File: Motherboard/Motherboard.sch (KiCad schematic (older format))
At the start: 0 parts

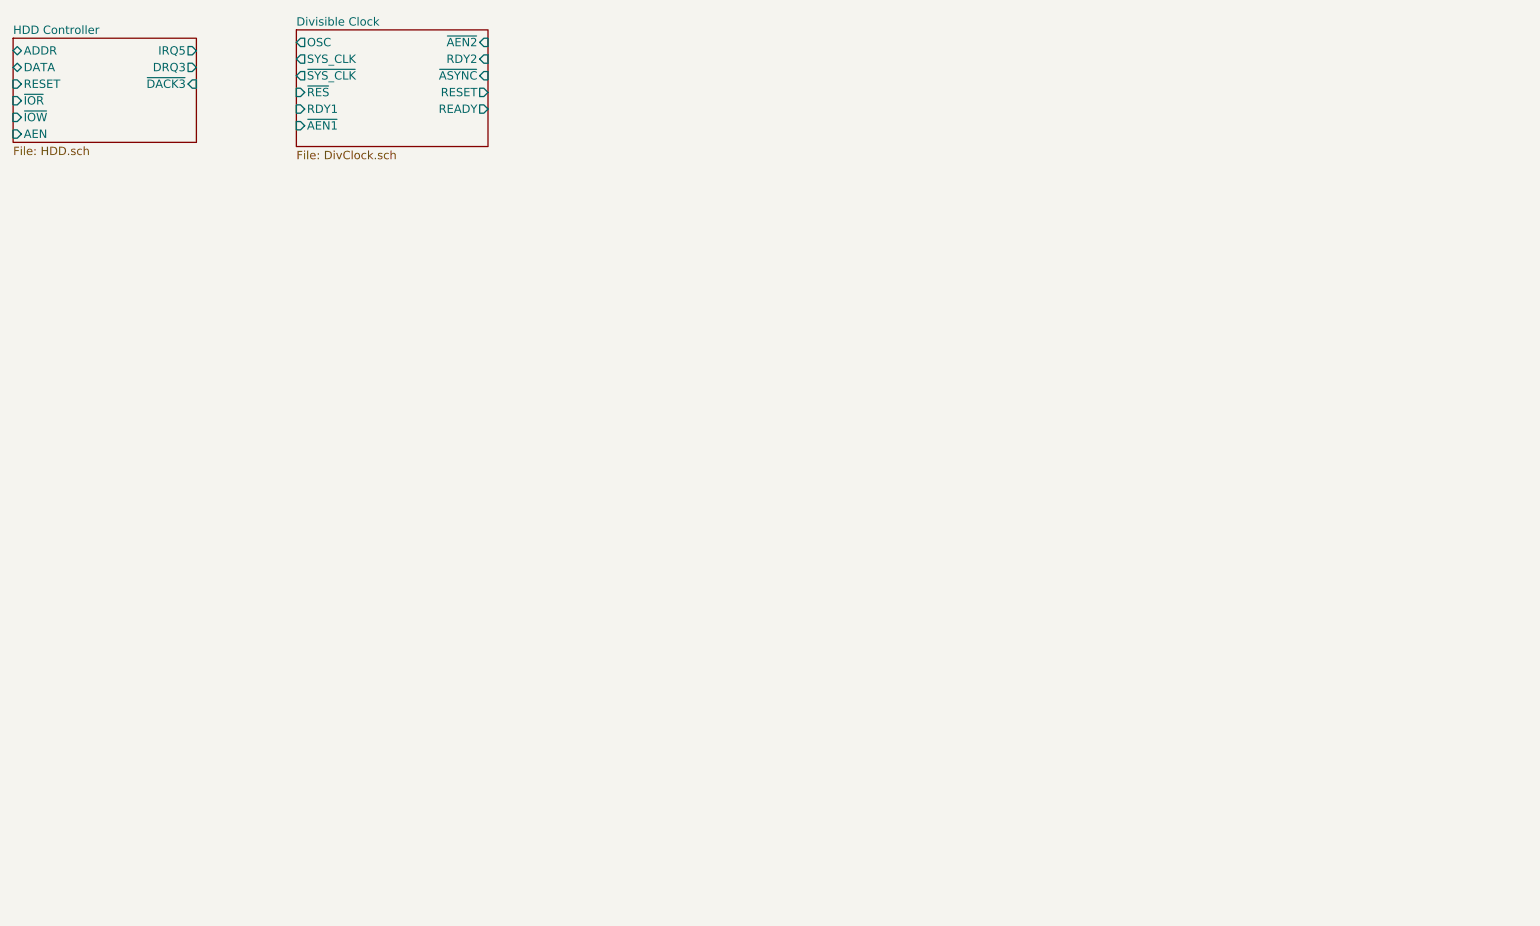
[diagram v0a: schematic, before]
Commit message: More work on Motherboard
Began work on PCB Routing
Began work on DMA
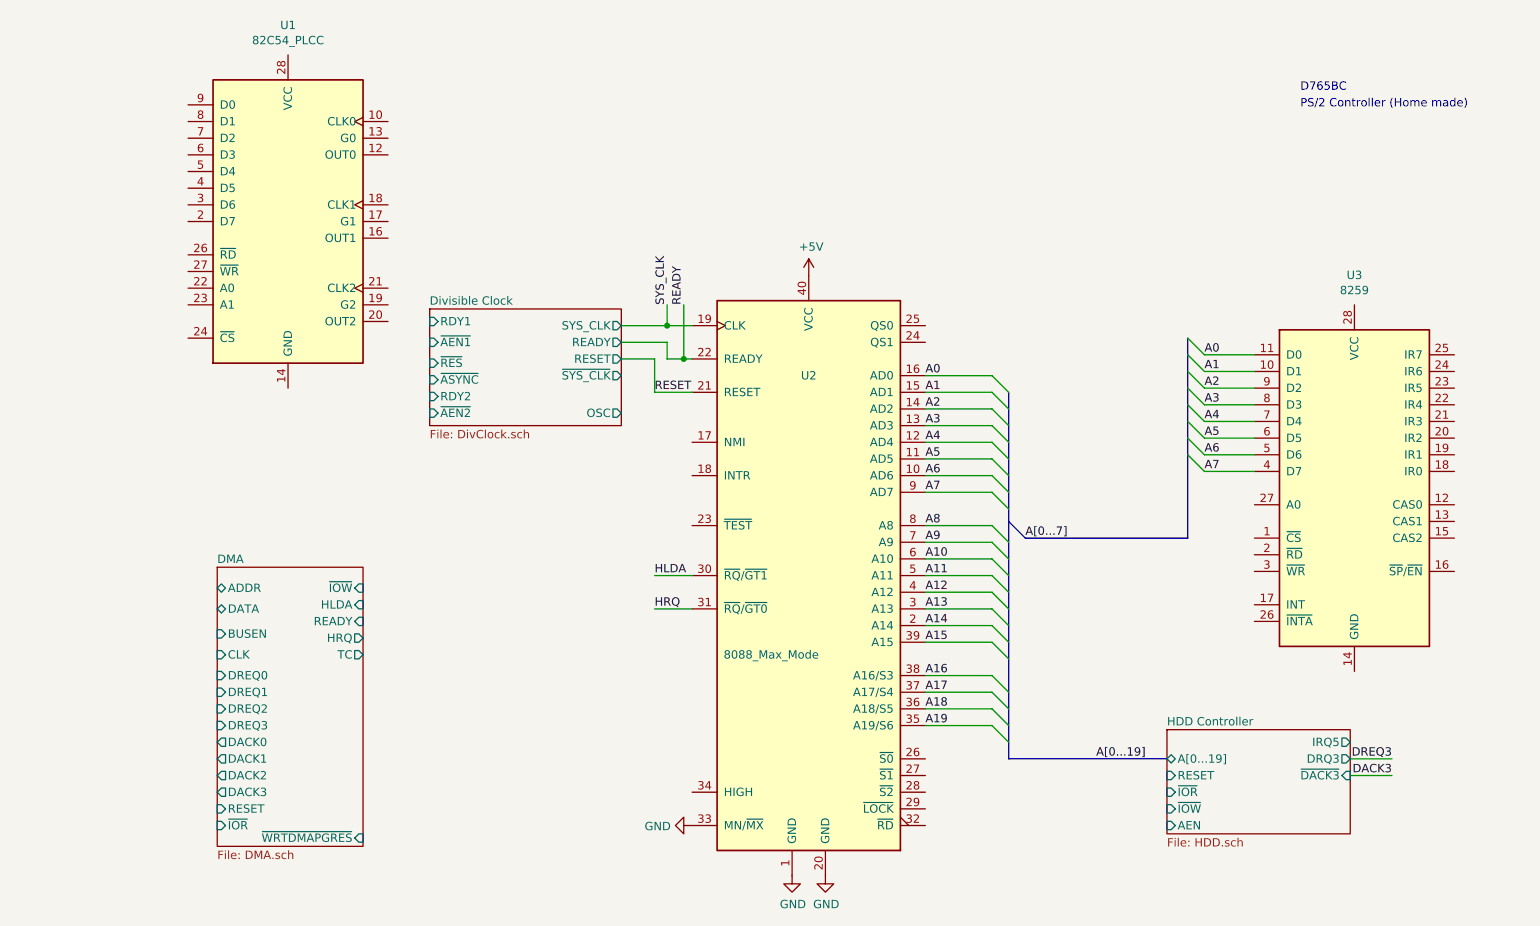
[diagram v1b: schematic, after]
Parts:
- added U1: 82C54_PLCC, Housings_DIP:DIP-28_W15.24mm_Socket, symbol Timer:82C54_PLCC
- added U2: 8088_Max_Mode, Housings_DIP:DIP-40_W15.24mm_Socket, symbol MCU_Intel:8088_Max_Mode
- added U3: 8259, Housings_DIP:DIP-28_W7.62mm_Socket, symbol Interface:8259
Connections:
- new net +5V: U2.40 (VCC)
- new net A0: U2.16 (AD0), U3.11 (D0)
- new net A1: U2.15 (AD1), U3.10 (D1)
- new net A10: U2.6 (A10)
- new net A11: U2.5 (A11)
- new net A12: U2.4 (A12)
- new net A13: U2.3 (A13)
- new net A14: U2.2 (A14)
- new net A15: U2.39 (A15)
- new net A16: U2.38 (A16/S3)
- new net A17: U2.37 (A17/S4)
- new net A18: U2.36 (A18/S5)
- new net A19: U2.35 (A19/S6)
- new net A2: U2.14 (AD2), U3.9 (D2)
- new net A3: U2.13 (AD3), U3.8 (D3)
- new net A4: U2.12 (AD4), U3.7 (D4)
- new net A5: U2.11 (AD5), U3.6 (D5)
- new net A6: U2.10 (AD6), U3.5 (D6)
- new net A7: U2.9 (AD7), U3.4 (D7)
- new net A8: U2.8 (A8)
- new net A9: U2.7 (A9)
- new net GND: U2.1 (GND), U2.20 (GND), U2.33 (MN/~MX~)
- new net HLDA: U2.30 (~RQ~/~GT1~)
- new net HRQ: U2.31 (~RQ~/~GT0~)
- new net READY: U2.22 (READY)
- new net RESET: U2.21 (RESET)
- new net SYS_CLK: U2.19 (CLK)
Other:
- note added: "D765BC"
- note added: "PS/2 Controller (Home made)"

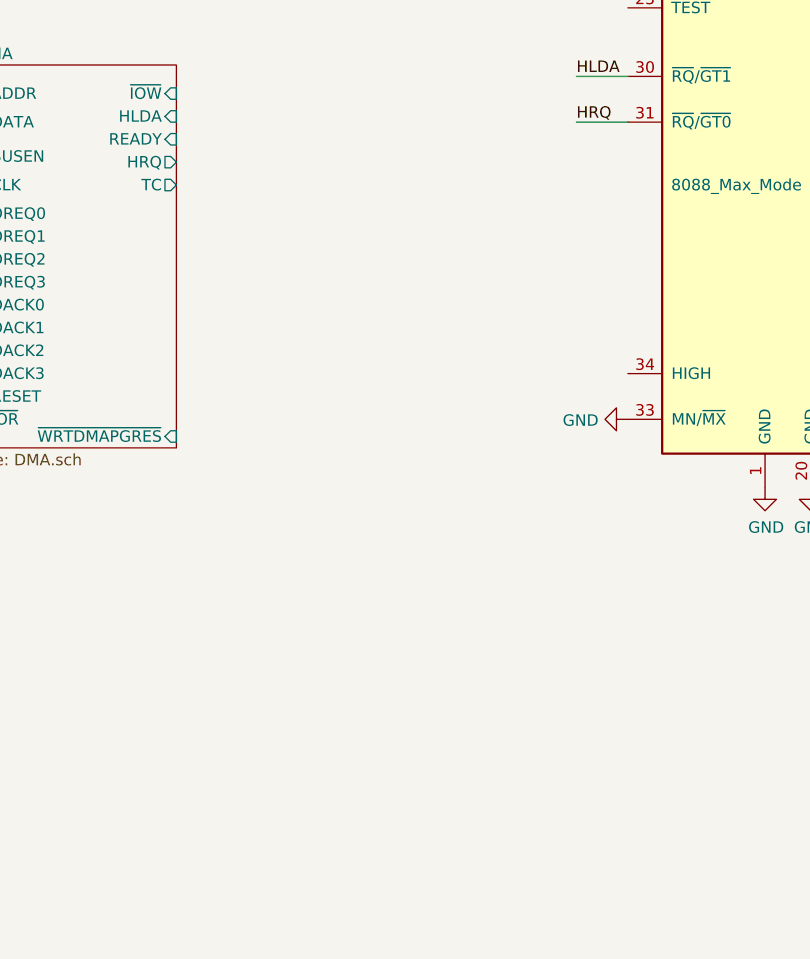
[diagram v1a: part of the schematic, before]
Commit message: Added ISA Footprint
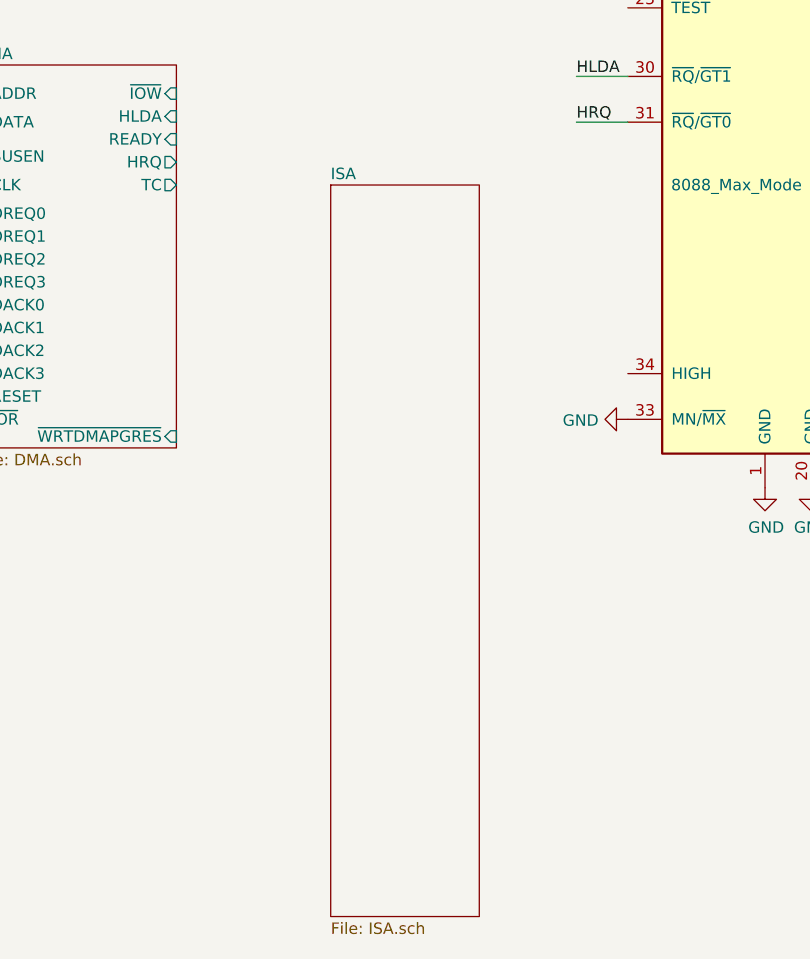
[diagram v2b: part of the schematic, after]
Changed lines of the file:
@@
 $Descr A4 11693 8268
 encoding utf-8
-Sheet 1 4
+Sheet 1 5
 Title "XT Clone Motherboard"
 Date ""
@@
 Wire Bus Line
 	6950 5100 7900 5100
+Text Label 7475 5100 0    50   ~ 0
+A[0...19]
+$Sheet
+S 3750 4475 650  3200
+U 5C18FA46
+F0 "ISA" 50
+F1 "ISA.sch" 50
+$EndSheet
 Wire Bus Line
 	8025 2575 8025 3775
 Wire Bus Line
 	6950 2900 6950 5100
-Text Label 7475 5100 0    50   ~ 0
-A[0...19]
 $EndSCHEMATC

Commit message: A VERY large sync...
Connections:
- net IO-Decoder/~S0: now reaches U2.26 (~S0~)
- net IO-Decoder/~S1: now reaches U2.27 (~S1~)
- net IO-Decoder/~S2: now reaches U2.28 (~S2~)
- net ~INTA: now reaches U3.26 (~INTA~)
- net A0 renamed AD0
- net AD0: no longer U3.11 (D0)
- net A1 renamed AD1
- net AD1: no longer U3.10 (D1)
- net A10 renamed AD10
- net A11 renamed AD11
- net A12 renamed AD12
- net A13 renamed AD13
- net A14 renamed AD14
- net A15 renamed AD15
- net A16 renamed AD16
- net A17 renamed AD17
- net A18 renamed AD18
- net A19 renamed AD19
- net A2 renamed AD2
- net AD2: no longer U3.9 (D2)
- net A3 renamed AD3
- net AD3: no longer U3.8 (D3)
- net A4 renamed AD4
- net AD4: no longer U3.7 (D4)
- net A5 renamed AD5
- net AD5: no longer U3.6 (D5)
- net A6 renamed AD6
- net AD6: no longer U3.5 (D6)
- net A7 renamed AD7
- net AD7: no longer U3.4 (D7)
- net A8 renamed AD8
- net A9 renamed AD9
- new net D0: U3.11 (D0)
- new net D1: U3.10 (D1)
- new net D2: U3.9 (D2)
- new net D3: U3.8 (D3)
- new net D4: U3.7 (D4)
- new net D5: U3.6 (D5)
- new net D6: U3.5 (D6)
- new net D7: U3.4 (D7)
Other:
- note added: "DCLK From IO Decode"
- moved on the sheet: U1, U3

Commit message: Large sync
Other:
- note removed: "D765BC"
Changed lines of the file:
@@
 EELAYER 26 0
 EELAYER END
-$Descr A4 11693 8268
+$Descr A3 16535 11693
 encoding utf-8
 Sheet 1 8
@@
 $EndDescr
 $Sheet
-S 9325 4200 1100 625
+S 8400 4650 1100 625
 U 5C0ABBCC
 F0 "HDD Controller" 50
 F1 "HDD.sch" 50
-F2 "RESET" I L 9325 4475 50
-F3 "~IOR" I L 9325 4575 50
-F4 "~IOW" I L 9325 4675 50
-F5 "AEN" I L 9325 4775 50
-F6 "IRQ5" O R 10425 4275 50
-F7 "DRQ3" O R 10425 4375 50
-F8 "~DACK3" I R 10425 4475 50
-F9 "A[0...19]" B L 9325 4375 50
+F2 "RESET" I L 8400 4925 50
+F3 "~IOR" I L 8400 5025 50
+F4 "~IOW" I L 8400 5125 50
+F5 "AEN" I L 8400 5225 50
+F6 "IRQ5" O R 9500 4725 50
+F7 "DRQ3" O R 9500 4825 50
+F8 "~DACK3" I R 9500 4925 50
+F9 "A[0...19]" B L 8400 4825 50
 $EndSheet
 $Sheet
@@
 	1    0    0    -1
 $EndComp
-Text Notes 8700 1100 0    50   ~ 0
-D765BC
 Text Notes 8700 1200 0    50   ~ 0
 PS/2 Controller (Home made)
-Text Label 10675 4375 2    50   ~ 0
+Text Label 9750 4825 2    50   ~ 0
 DREQ3
 Wire Wire Line
-	10425 4375 10675 4375
+	9500 4825 9750 4825
 Wire Wire Line
 	4900 2500 4900 2375
@@
 SYS_CLK
 Wire Wire Line
-	10425 4475 10675 4475
-Text Label 10675 4475 2    50   ~ 0
+	9500 4925 9750 4925
+Text Label 9750 4925 2    50   ~ 0
 DACK3
 Text Label 4825 2900 0    50   ~ 0
@@
 F16 "D[0...7]" O R 7875 5800 50
 F17 "A[0...19]" O R 7875 5700 50
+F18 "DCLK" O R 7875 5900 50
 $EndSheet
 Wire Bus Line
@@
 A[0...19]
 Text Label 9450 3050 1    50   ~ 0
-D[0...7]
+XD[0...7]
+Text Notes 975  4450 0    50   ~ 0
+DCLK From IO Decode
+Wire Wire Line
+	7875 5900 8275 5900
 Wire Bus Line
 	1050 4075 2200 4075
@@
 Wire Bus Line
 	6950 2900 6950 5100
-Text Notes 1325 4450 0    50   ~ 0
-DCLK From IO Decode
+Text Label 8275 5900 2    50   ~ 0
+DCLK
+Text Label 1950 4475 0    50   ~ 0
+DCLK
 $EndSCHEMATC

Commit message: Work on motherboard  - Integrating glue logic into CPLD  - Began work on routing
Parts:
- U1: footprint Housings_DIP:DIP-28_W15.24mm_Socket -> Housings_LCC:PLCC-28_THT-Socket
- U2: value 8088_Max_Mode -> 8088
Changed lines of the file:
@@
 P 5750 4000
 F 0 "U2" H 5750 5200 50  0000 C CNN
-F 1 "8088_Max_Mode" H 5525 3525 50  0000 C CNN
+F 1 "8088" H 5525 3525 50  0000 C CNN
 F 2 "Housings_DIP:DIP-40_W15.24mm_Socket" H 5800 4100 50  0001 C CIN
 F 3 "http://datasheets.chipdb.org/Intel/x86/808x/datashts/8088/231456-006.pdf" H 5750 4050 50  0001 C CNN
@@
 F 0 "U1" H 1325 3053 50  0000 C CNN
 F 1 "82C54_PLCC" H 1325 2962 50  0000 C CNN
-F 2 "Housings_DIP:DIP-28_W15.24mm_Socket" H 1375 2125 50  0001 C CNN
+F 2 "Housings_LCC:PLCC-28_THT-Socket" H 1375 2125 50  0001 C CNN
 F 3 "http://download.intel.com/design/archives/periphrl/docs/23124406.pdf" H 875 2775 50  0001 C CNN
 	1    1325 1875
@@
 D7
 $Sheet
-S 3750 4475 650  3200
+S 3750 4500 650  3200
 U 5C18FA46
 F0 "ISA" 50
 F1 "ISA.sch" 50
+F2 "RESET" I L 3750 4600 50
+F3 "OSC" I L 3750 4675 50
+F4 "DRQ[0...3]" I L 3750 4750 50
+F5 "~DACK~[0...3]" I L 3750 4825 50
+F6 "CLK" I L 3750 4900 50
+F7 "~IOW" I L 3750 4975 50
+F8 "IRQ[3...7]" I L 3750 5050 50
+F9 "TC" I L 3750 5125 50
+F10 "ALE" I L 3750 5200 50
+F11 "IO" I L 3750 5275 50
+F12 "D[0...7]" I L 3750 5350 50
+F13 "A[0...19]" I L 3750 5425 50
+F14 "IO_READY" I L 3750 5500 50
+F15 "AEN" I L 3750 5575 50
+F16 "~SMEMW" I L 3750 5650 50
+F17 "~SMEMR" I L 3750 5725 50
 $EndSheet
 $Sheet
@@
 Wire Wire Line
 	7875 5900 8275 5900
-Wire Bus Line
-	1050 4075 2200 4075
-Wire Bus Line
-	9450 1850 9450 3050
-Wire Bus Line
-	6950 2900 6950 5100
 Text Label 8275 5900 2    50   ~ 0
 DCLK
 Text Label 1950 4475 0    50   ~ 0
 DCLK
+Wire Bus Line
+	1050 4075 2200 4075
+Wire Bus Line
+	9450 1850 9450 3050
+Wire Bus Line
+	6950 2900 6950 5100
 $EndSCHEMATC

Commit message: Some missed changes
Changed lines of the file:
@@
 Wire Bus Line
 	6950 2900 6950 5100
+Text Label 6950 5075 2    50   ~ 0
+AD[0...19]
 $EndSCHEMATC

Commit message: Large sync
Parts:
- added U11: 8087, Housings_DIP:DIP-40_W15.24mm_Socket, symbol MCU_Intel:8087
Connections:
- net +5V: now also U11.40 (VCC)
- net AD0: now also U11.16 (AD0)
- net AD1: now also U11.15 (AD1)
- net AD10: now also U11.6 (AD10)
- net AD11: now also U11.5 (AD11)
- net AD12: now also U11.4 (AD12)
- net AD13: now also U11.3 (AD13)
- net AD14: now also U11.2 (AD14)
- net AD15: now also U11.39 (AD15)
- net AD16: now also U11.38 (A16/S3)
- net AD17: now also U11.37 (A17/S4)
- net AD18: now also U11.36 (A18/S5)
- net AD19: now also U11.35 (A19/S6)
- net AD2: now also U11.14 (AD2)
- net AD3: now also U11.13 (AD3)
- net AD4: now also U11.12 (AD4)
- net AD5: now also U11.11 (AD5)
- net AD6: now also U11.10 (AD6)
- net AD7: now also U11.9 (AD7)
- net AD8: now also U11.8 (AD8)
- net AD9: now also U11.7 (AD9)
- net GND: now also U11.1 (GND), U11.20 (GND)
- net READY: now also U11.22 (READY)
- net RESET: now also U11.21 (RESET)
- net SYS_CLK: now also U11.19 (CLK)
- net IRQ1: now reaches U3.19 (IR1)
- net IRQ3: now reaches U3.21 (IR3)
- net IRQ4: now reaches U3.22 (IR4)
- net IRQ5: now reaches U3.23 (IR5)
- net IRQ6: now reaches U3.24 (IR6)
- net IRQ7: now reaches U3.25 (IR7)
- net IO-Decoder/~S0 renamed ~S0
- net ~S0: now also U11.26 (~S0~)
- net IO-Decoder/~S1 renamed ~S1
- net ~S1: now also U11.27 (~S1~)
- net IO-Decoder/~S2 renamed ~S2
- net ~S2: now also U11.28 (~S2~)
- new net N.P.NPI: U11.32 (INT)
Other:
- note removed: "PS/2 Controller (Home made)"
